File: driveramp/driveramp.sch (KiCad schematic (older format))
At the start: 56 parts, among them J1 SMA, J2 SMA, P1 FAULT, P2 CONN_2, T1 MABA-011002, T2 2x Fair-Rite 2843006802, coax, U1 LM2936HVBMA-5.0, U2 MRFE6VP100H

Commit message: updated tr board to remove DNP components
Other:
- note added: "2-1445053-2"
- note added: "3-794636-2"
- note added: "class AB driver amplifier, 2 MHz to 20 MHz\nidsq of 400 mA at Vdd 50 V"
- note removed: "class AB driver amplifier, 2 MHz to 20 MHz\nidsq of 200 mA at Vdd 50 V"
- moved on the sheet: TH1
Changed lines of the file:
@@
 F 3 "" H 2650 4400 60  0000 C CNN
 	1    2650 4400
-	1    0    0    -1
+	-1   0    0    1
 $EndComp
 Text Notes 6850 2500 0    118  ~ 0
-class AB driver amplifier, 2 MHz to 20 MHz\nidsq of 200 mA at Vdd 50 V
+class AB driver amplifier, 2 MHz to 20 MHz\nidsq of 400 mA at Vdd 50 V
 Text Notes 500  6550 0    60   ~ 0
 see http://application-notes.digchip.com/147/147-47845.pdf for description of bias network\nsee freescale AN1643\n
@@
 Text Notes 5950 1550 0    118  ~ 0
 see http://www.nxp.com/documents/report/R_10032.pdf
+Text Notes 7900 3100 0    60   ~ 0
+2-1445053-2
+Text Notes 3400 1950 0    60   ~ 0
+3-794636-2
 $EndSCHEMATC

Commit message: moved agc coupled signal splitting off-board
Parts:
- removed C10, C29, C3: 2.2uF, Capacitors_SMD:c_0805, symbol C
- removed C15, C6: JMP, Capacitors_SMD:c_0805, symbol C
- removed C23, C24: 20nF, Capacitors_SMD:c_0805, symbol C
- removed C26: ??, Capacitors_SMD:c_0805, symbol C
- removed D2: ZENERsmall, Diodes_SMD:Diode-SMB_Handsoldering, symbol ZENERsmall
- added C15, C6: 56uF, Capacitors_SMD:c_elec_10x10, symbol CAPAPOL
- added C35: 2.2uF, Capacitors_SMD:c_0805, symbol C
- added R7: 2.49 ohm, 2 W(RHC2512FT2R49), SMD_Packages:SM2512, symbol R
- added U3: TL783, SMD_Packages:DPAK3, symbol LM317AMDT
- C17, C21: value ?? -> DNP
- D1: footprint Diodes_SMD:Diode-SMB_Handsoldering -> local:DUAL_DIODE
- P1, P2: footprint Connect:PINHEAD1-2 -> local:2-1445053-2
- R1, R4: value 1k 3W -> 1k 3W (DNP)
- RV1: footprint Potentiometers:Potentiometer_Bourns_3296Y_3-8Zoll_Angular_ScrewUp -> local:POT_SMD
- TH1: footprint Resistors_ThroughHole:Resistor_Vertical_RM5mm -> local:NTC_HSMOUNT
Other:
- note added: "current limiting using linear regulator to absorb startup transients..\nI = Vref/R, Vref = 1.25 V"
- note added: "max pulse length: 5 ms\n"
- moved on the sheet: P2

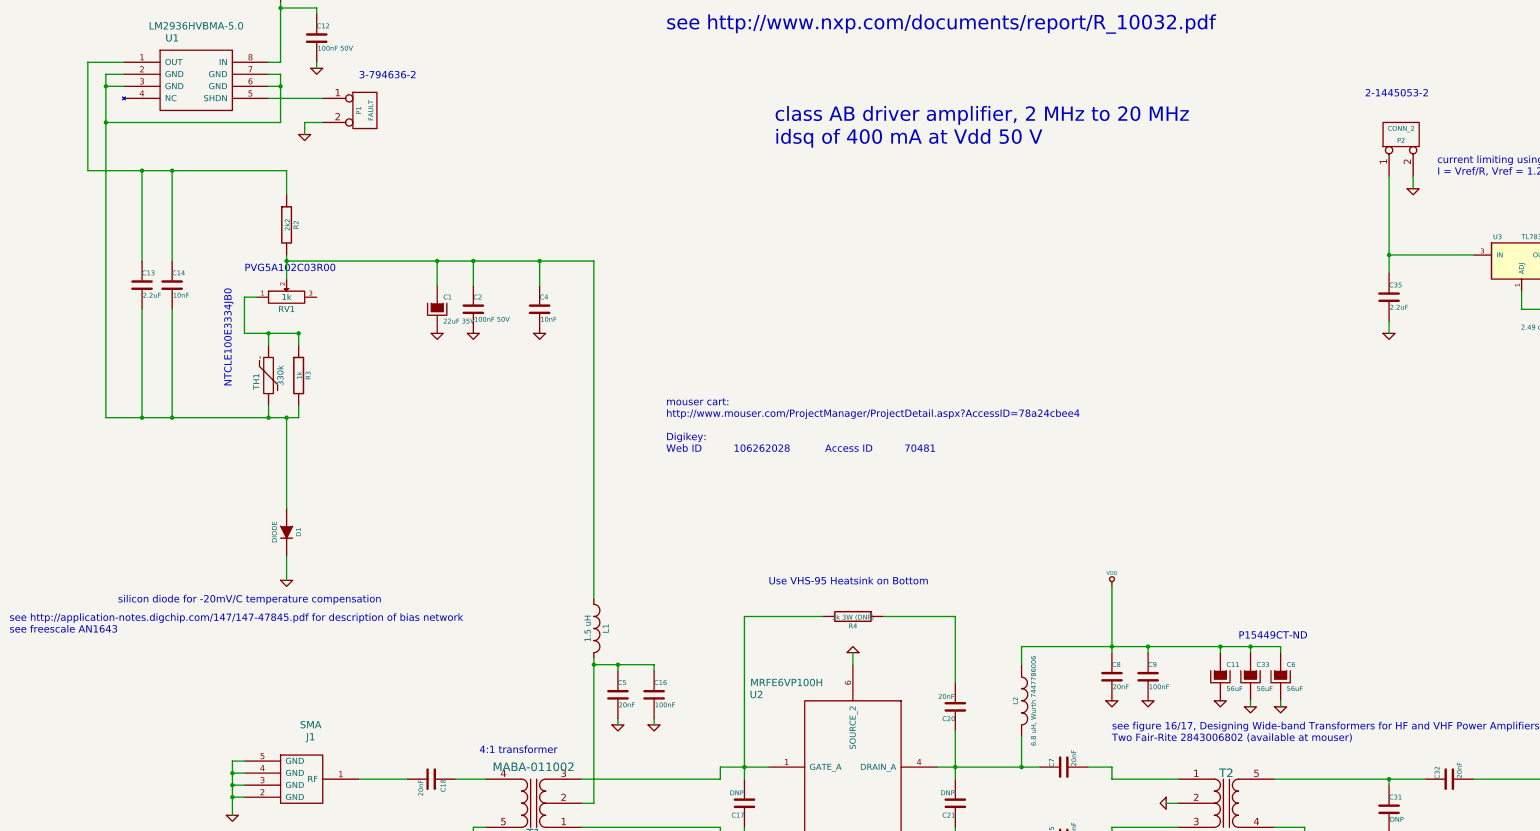
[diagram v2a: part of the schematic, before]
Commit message: polishing agc, tr, and driver amp for next revisions. moved all bottom layer signal traces to top layer on driver amp
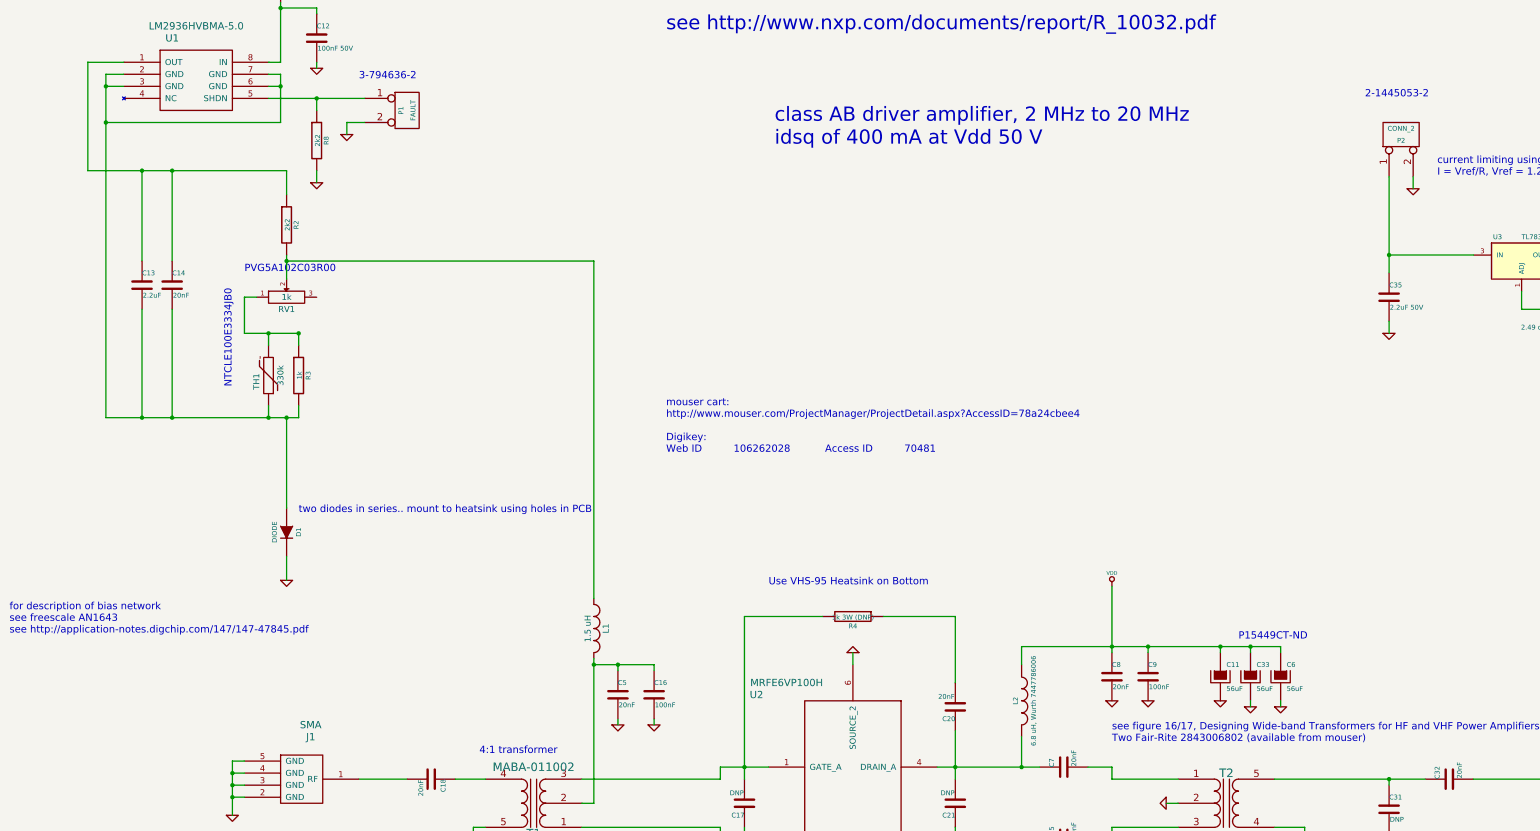
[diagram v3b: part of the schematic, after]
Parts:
- removed C1: 22uF 35V, Capacitors_SMD:c_1210, symbol CAPAPOL
- removed C2: 100nF 50V, Capacitors_SMD:c_0805, symbol C
- removed C4: 10nF, Capacitors_SMD:c_0805, symbol C
- added R8: 2k2, SMD_Packages:SM0805, symbol R
- C14: value 10nF -> 20nF
- C35: value 2.2uF -> 2.2uF 50V
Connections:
- net GND: now also R8.2
- net at P1.1 (P1), U1.5 (SHDN): now also R8.1
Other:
- note added: "for description of bias network\nsee freescale AN1643\nsee http://application-notes.digchip.com/147/147-47845.pdf \n"
- note added: "see figure 16/17, Designing Wide-band Transformers for HF and VHF Power Amplifiers by Chris Trask, N7ZWY\nTwo Fair-Rite 2843006802 (available from mouser)"
- note added: "two diodes in series.. mount to heatsink using holes in PCB"
- note removed: "see figure 16/17, Designing Wide-band Transformers for HF and VHF Power Amplifiers by Chris Trask, N7ZWY\nTwo Fair-Rite 2843006802 (available at mouser)"
- note removed: "see http://application-notes.digchip.com/147/147-47845.pdf for description of bias network\nsee freescale AN1643\n"
- note removed: "silicon diode for -20mV/C temperature compensation\n"
- moved on the sheet: P1

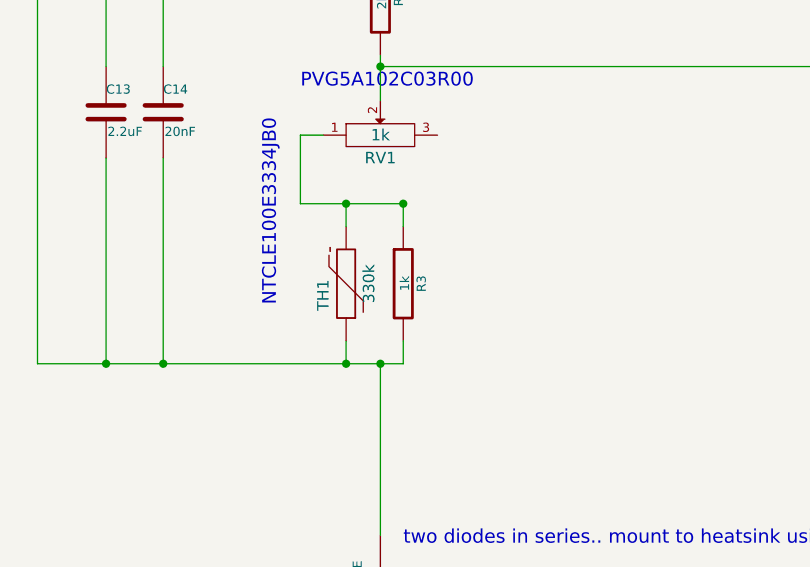
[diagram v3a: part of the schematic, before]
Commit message: updated bias network values on driver amp
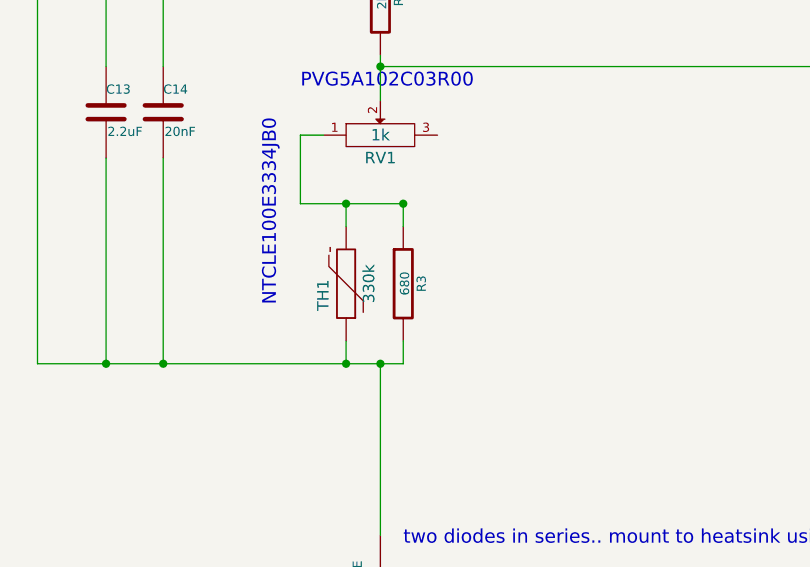
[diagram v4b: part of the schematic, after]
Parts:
- R3: value 1k -> 680
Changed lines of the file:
@@
 P 2900 4400
 F 0 "R3" V 2980 4400 40  0000 C CNN
-F 1 "1k" V 2907 4401 40  0000 C CNN
+F 1 "680" V 2907 4401 40  0000 C CNN
 F 2 "SMD_Packages:SM0805" V 2830 4400 30  0001 C CNN
 F 3 "" H 2900 4400 30  0000 C CNN

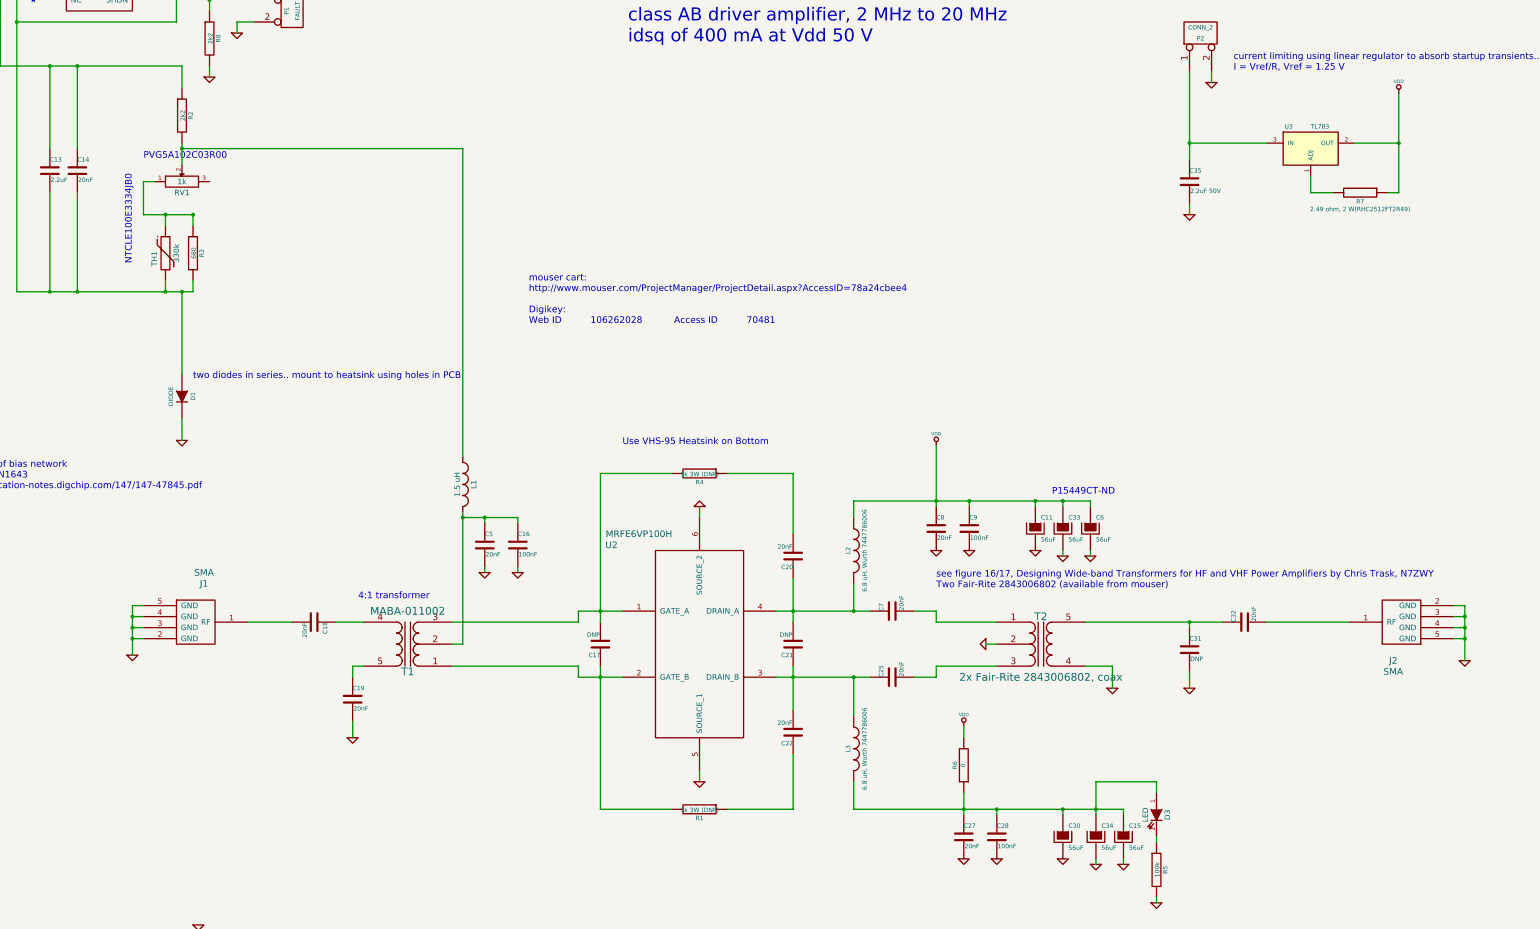
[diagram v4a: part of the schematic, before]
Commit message: fixed bugs in driver amp - fixed current limiter, eliminated need for 50v jumper
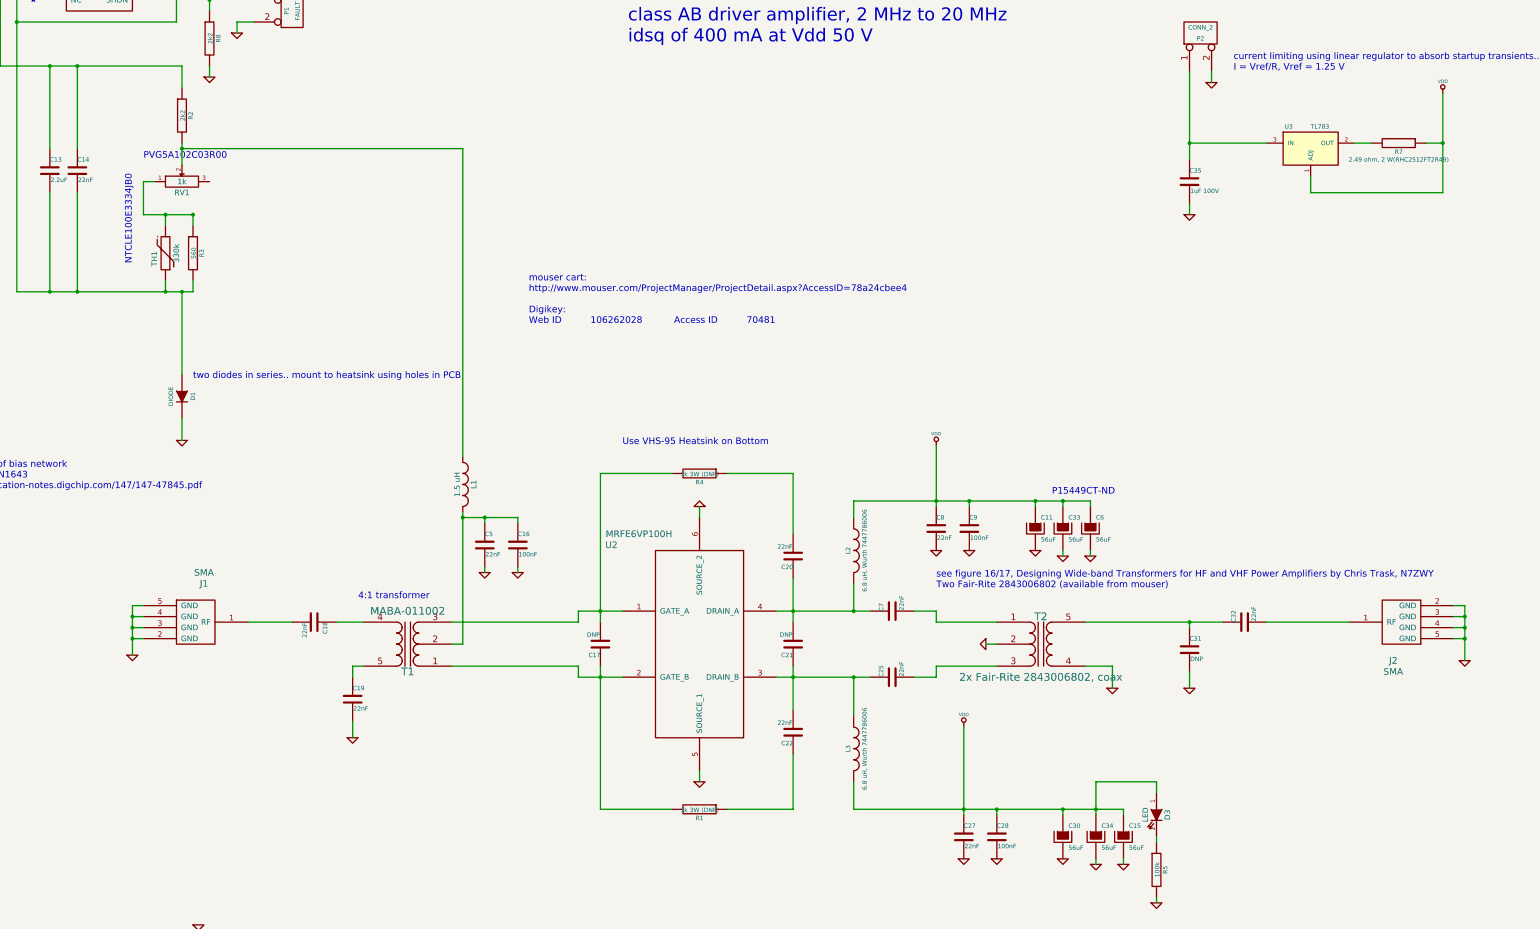
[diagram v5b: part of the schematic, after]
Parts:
- removed R6: 0, Resistors_ThroughHole:Resistor_Horizontal_RM25mm, symbol R
- C14, C18, C19, C20, C22, C25, C27, C32, C5, C7, C8: value 20nF -> 22nF
- C35: value 2.2uF 50V -> 1uF 100V
- R3: value 680 -> 560
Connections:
- net VDD: now also C15.1, C27.1, C28.1, C30.1, C34.1, D3.1 (A), L3.2, U3.1 (ADJ); no longer U3.2 (OUT)
- net at R7.2: now also U3.2 (OUT); no longer U3.1 (ADJ)
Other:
- moved on the sheet: R7
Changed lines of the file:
@@
 P 9250 7650
 F 0 "C7" H 9250 7750 40  0000 L CNN
-F 1 "20nF" H 9256 7565 40  0000 L CNN
+F 1 "22nF" H 9256 7565 40  0000 L CNN
 F 2 "Capacitors_SMD:c_0805" H 9288 7500 30  0001 C CNN
 F 3 "~" H 9250 7650 60  0000 C CNN
@@
 P 9650 6900
 F 0 "C8" H 9650 7000 40  0000 L CNN
-F 1 "20nF" H 9656 6815 40  0000 L CNN
+F 1 "22nF" H 9656 6815 40  0000 L CNN
 F 2 "Capacitors_SMD:c_0805" H 9688 6750 30  0001 C CNN
 F 3 "~" H 9650 6900 60  0000 C CNN
@@
 P 2900 4400
 F 0 "R3" V 2980 4400 40  0000 C CNN
-F 1 "680" V 2907 4401 40  0000 C CNN
+F 1 "560" V 2907 4401 40  0000 C CNN
 F 2 "SMD_Packages:SM0805" V 2830 4400 30  0001 C CNN
 F 3 "" H 2900 4400 30  0000 C CNN
@@
 P 1850 3650
 F 0 "C14" H 1850 3750 40  0000 L CNN
-F 1 "20nF" H 1856 3565 40  0000 L CNN
+F 1 "22nF" H 1856 3565 40  0000 L CNN
 F 2 "Capacitors_SMD:c_0805" H 1888 3500 30  0001 C CNN
 F 3 "~" H 1850 3650 60  0000 C CNN
@@
 P 4350 8450
 F 0 "C19" H 4350 8550 40  0000 L CNN
-F 1 "20nF" H 4356 8365 40  0000 L CNN
+F 1 "22nF" H 4356 8365 40  0000 L CNN
 F 2 "Capacitors_SMD:c_0805" H 4388 8300 30  0001 C CNN
 F 3 "~" H 4350 8450 60  0000 C CNN
@@
 P 4000 7750
 F 0 "C18" H 4000 7850 40  0000 L CNN
-F 1 "20nF" H 4006 7665 40  0000 L CNN
+F 1 "22nF" H 4006 7665 40  0000 L CNN
 F 2 "Capacitors_SMD:c_0805" H 4038 7600 30  0001 C CNN
 F 3 "~" H 4000 7750 60  0000 C CNN
@@
 P 8350 7150
 F 0 "C20" H 8350 7250 40  0000 L CNN
-F 1 "20nF" H 8356 7065 40  0000 L CNN
+F 1 "22nF" H 8356 7065 40  0000 L CNN
 F 2 "Capacitors_SMD:c_0805" H 8388 7000 30  0001 C CNN
 F 3 "~" H 8350 7150 60  0000 C CNN
@@
 P 8350 8750
 F 0 "C22" H 8350 8850 40  0000 L CNN
-F 1 "20nF" H 8356 8665 40  0000 L CNN
+F 1 "22nF" H 8356 8665 40  0000 L CNN
 F 2 "Capacitors_SMD:c_0805" H 8388 8600 30  0001 C CNN
 F 3 "~" H 8350 8750 60  0000 C CNN
@@
 P 5550 7050
 F 0 "C5" H 5550 7150 40  0000 L CNN
-F 1 "20nF" H 5556 6965 40  0000 L CNN
+F 1 "22nF" H 5556 6965 40  0000 L CNN
 F 2 "Capacitors_SMD:c_0805" H 5588 6900 30  0001 C CNN
 F 3 "~" H 5550 7050 60  0000 C CNN
@@
 P 9250 8250
 F 0 "C25" H 9250 8350 40  0000 L CNN
-F 1 "20nF" H 9256 8165 40  0000 L CNN
+F 1 "22nF" H 9256 8165 40  0000 L CNN
 F 2 "Capacitors_SMD:c_0805" H 9288 8100 30  0001 C CNN
 F 3 "~" H 9250 8250 60  0000 C CNN
@@
 P 9900 9700
 F 0 "C27" H 9900 9800 40  0000 L CNN
-F 1 "20nF" H 9906 9615 40  0000 L CNN
+F 1 "22nF" H 9906 9615 40  0000 L CNN
 F 2 "Capacitors_SMD:c_0805" H 9938 9550 30  0001 C CNN
 F 3 "~" H 9900 9700 60  0000 C CNN
@@
 P 12450 7750
 F 0 "C32" H 12450 7850 40  0000 L CNN
-F 1 "20nF" H 12456 7665 40  0000 L CNN
+F 1 "22nF" H 12456 7665 40  0000 L CNN
 F 2 "Capacitors_SMD:c_0805" H 12488 7600 30  0001 C CNN
 F 3 "~" H 12450 7750 60  0000 C CNN
@@
 L VDD #PWR31
 U 1 1 53A9D510
-P 13850 2950
-F 0 "#PWR31" H 13850 3050 30  0001 C CNN
-F 1 "VDD" H 13850 3060 30  0000 C CNN
-F 2 "" H 13850 2950 60  0000 C CNN
-F 3 "" H 13850 2950 60  0000 C CNN
-	1    13850 2950
+P 14250 2950
+F 0 "#PWR31" H 14250 3050 30  0001 C CNN
+F 1 "VDD" H 14250 3060 30  0000 C CNN
+F 2 "" H 14250 2950 60  0000 C CNN
+F 3 "" H 14250 2950 60  0000 C CNN
+	1    14250 2950
 	1    0    0    -1
 $EndComp
@@
 $EndComp
 $Comp
-L R R6
-U 1 1 53AA11BC
-P 9900 9050
-F 0 "R6" V 9980 9050 40  0000 C CNN
-F 1 "0" V 9907 9051 40  0000 C CNN
-F 2 "Resistors_ThroughHole:Resistor_Horizontal_RM25mm" V 9830 9050 30  0001 C CNN
-F 3 "" H 9900 9050 30  0000 C CNN
-	1    9900 9050
-	-1   0    0    1
-$EndComp
-$Comp
 L VDD #PWR15
 U 1 1 53AA1331
@@
 P 11950 3750
 F 0 "C35" H 11950 3850 40  0000 L CNN
-F 1 "2.2uF 50V" H 11956 3665 40  0000 L CNN
+F 1 "1uF 100V" H 11956 3665 40  0000 L CNN
 F 2 "Capacitors_SMD:c_0805" H 11988 3600 30  0001 C CNN
 F 3 "~" H 11950 3750 60  0000 C CNN
@@
 	10800 7150 10800 7100
 Wire Wire Line
-	9900 9300 9900 9500
-Wire Wire Line
-	9900 8700 9900 8800
+	9900 8700 9900 9500
 Wire Wire Line
 	11650 9200 11100 9200
@@
 Connection ~ 11950 3400
 Wire Wire Line
-	13850 2950 13850 3850
-Wire Wire Line
-	13850 3400 13450 3400
+	14250 3850 14250 2950
 $Comp
 L R R7
 U 1 1 53CF6B6B
-P 13500 3850
-F 0 "R7" V 13580 3850 40  0000 C CNN
-F 1 "2.49 ohm, 2 W(RHC2512FT2R49)" V 13650 3850 40  0000 C CNN
-F 2 "SMD_Packages:SM2512" V 13430 3850 30  0001 C CNN
-F 3 "" H 13500 3850 30  0000 C CNN
-	1    13500 3850
+P 13850 3400
+F 0 "R7" V 13930 3400 40  0000 C CNN
+F 1 "2.49 ohm, 2 W(RHC2512FT2R49)" V 14000 3400 40  0000 C CNN
+F 2 "SMD_Packages:SM2512" V 13780 3400 30  0001 C CNN
+F 3 "" H 13850 3400 30  0000 C CNN
+	1    13850 3400
 	0    1    1    0
 $EndComp
@@
 	13050 3700 13050 3850
 Wire Wire Line
-	13050 3850 13250 3850
-Wire Wire Line
-	13850 3850 13750 3850
-Connection ~ 13850 3400
+	13050 3850 14250 3850
 Text Notes 12350 2750 0    60   ~ 0
 current limiting using linear regulator to absorb startup transients..\nI = Vref/R, Vref = 1.25 V
@@
 	3050 2200 3050 2100
 Connection ~ 3050 2100
+Wire Wire Line
+	13450 3400 13600 3400
+Wire Wire Line
+	14100 3400 14250 3400
+Connection ~ 14250 3400
 $EndSCHEMATC
